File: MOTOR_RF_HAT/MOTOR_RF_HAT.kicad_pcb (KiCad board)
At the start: 6 copper layers, 32 x 65 mm, 107 parts, among them J1 SMA, J2 SMA, J3 Raspberry_Pi_2_3, J4 Conn_01x01, J5 Conn_01x01, Q1 BSS138, U1 CC1200RHBR, U2 CC1200RHBR, U3 RaspberryPi_Pico, U4 XT30PW-M, U5 LMR51420YFDDCR, Y1 40MHz, Y2 40MHz

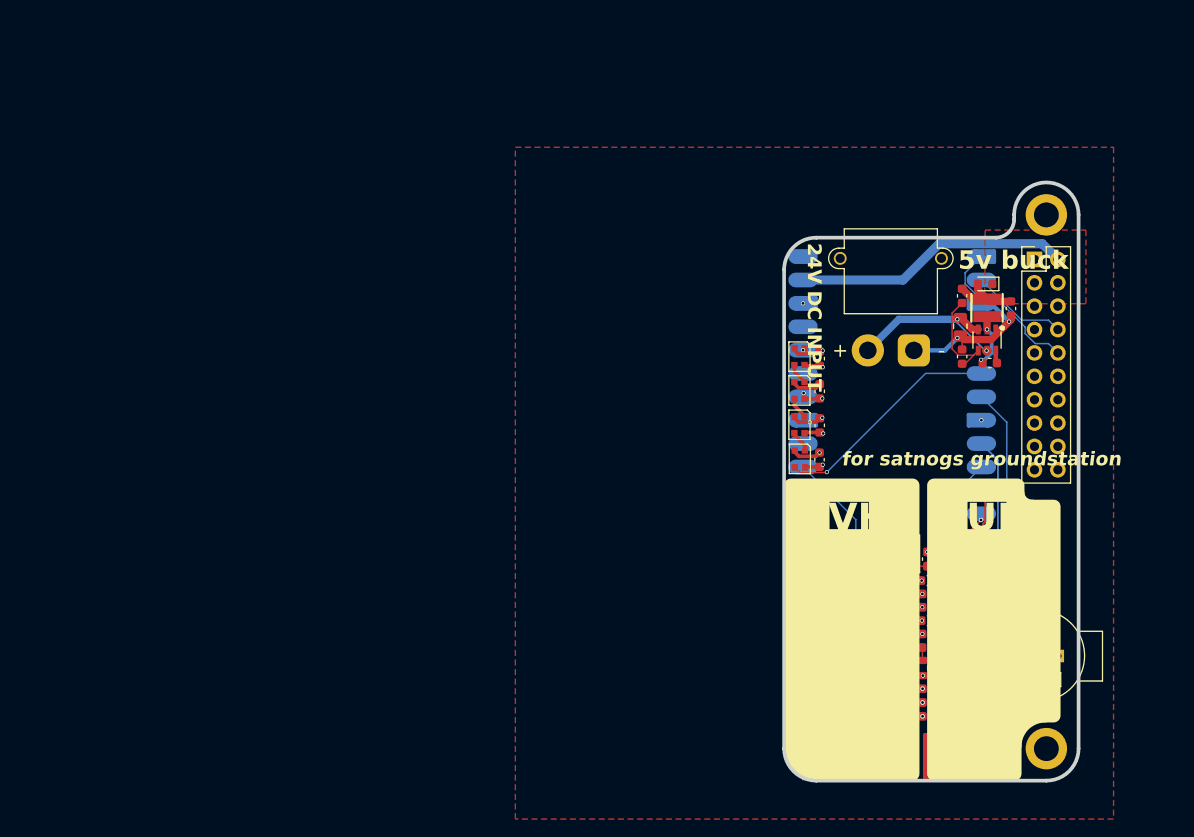
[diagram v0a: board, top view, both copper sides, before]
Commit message: MOTOR_RF_HAT: assign components:smallpad to all TestPoint_Small
Assigned local smallpad footprint to 8 TestPoint_Small instances:
- 7 in solder_pads.kicad_sch
- 1 in root schematic (TP19)

Co-Authored-By: Claude Opus 4.6 (1M context) <noreply@anthropic.com>
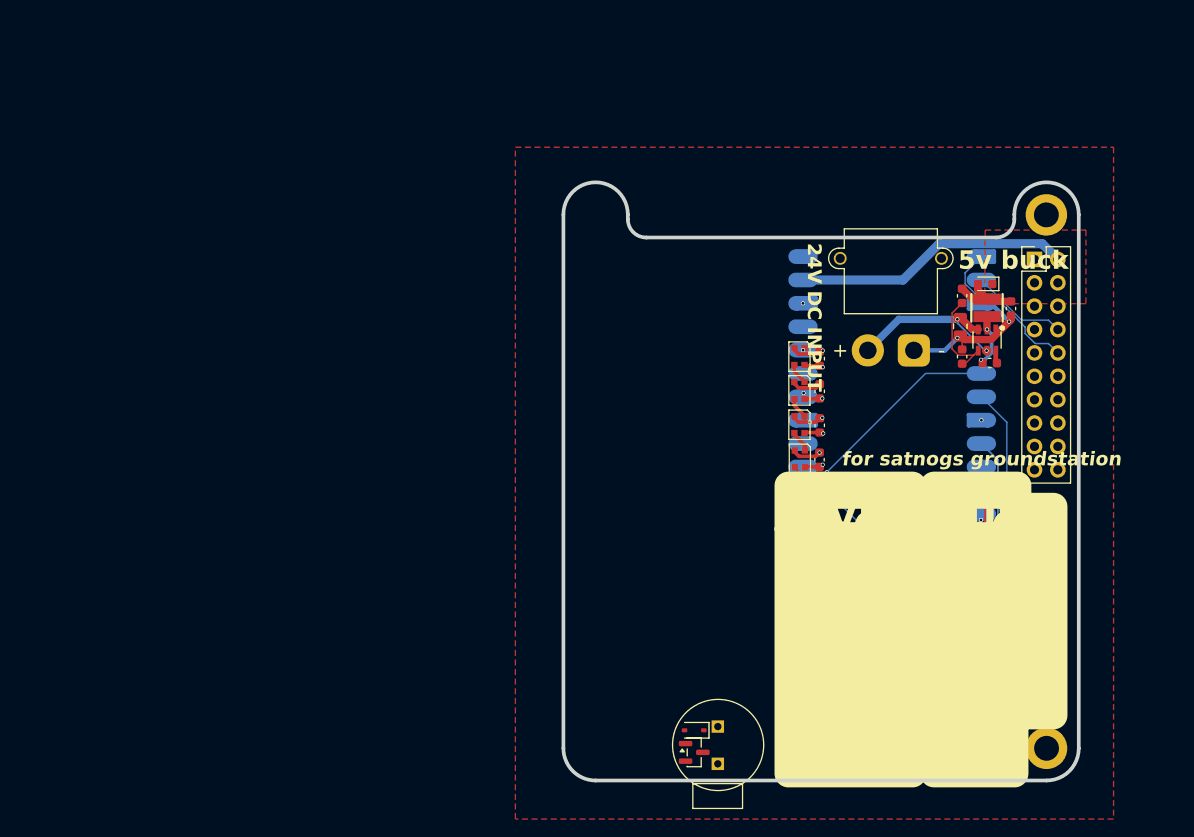
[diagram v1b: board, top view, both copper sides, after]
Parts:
- moved Q1 39.1 mm to (176.4, 122.8), turned to 0 degrees
- moved J5 38.8 mm to (179.0, 124.0), turned to 180 degrees
- moved D2 36.3 mm to (176.4, 120.4), turned to 180 degrees
- moved J4 33.8 mm to (179.0, 120.0), turned to 180 degrees
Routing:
- net Net-(D2-A): track 5.55 -> 0.00 mm
- net +3V3: track 66.8 -> 65.1 mm, vias 36 -> 35
- net GND: vias 63 -> 62
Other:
- board size 32 x 65 mm -> 56 x 65 mm

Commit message: MOTOR_RF_HAT: add TestPoint lib alias to fix persistent smallpad errors
KiCad's lib_symbols cache keeps reverting footprint refs to
TestPoint:smallpad on save. Added TestPoint as a footprint library
alias pointing to components.pretty so both TestPoint:smallpad and
components:smallpad resolve to the same local footprint.

Co-Authored-By: Claude Opus 4.6 (1M context) <noreply@anthropic.com>
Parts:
- added C60: 10uF, Capacitor_SMD:C_0805_2012Metric_Pad1.18x1.45mm_HandSolder, F.Cu at (120.2, 100.6)
- added C61: 10uF, Capacitor_SMD:C_0805_2012Metric_Pad1.18x1.45mm_HandSolder, F.Cu at (120.2, 103.6)
- added C62: 10uF, Capacitor_SMD:C_0805_2012Metric_Pad1.18x1.45mm_HandSolder, F.Cu at (120.2, 106.7)
- added C63: 100nF, Capacitor_SMD:C_0805_2012Metric_Pad1.18x1.45mm_HandSolder, F.Cu at (120.2, 109.7)
- added C64: 10uF, Capacitor_SMD:C_0805_2012Metric_Pad1.18x1.45mm_HandSolder, F.Cu at (104.9, 100.6)
- added C65: 10uF, Capacitor_SMD:C_0805_2012Metric_Pad1.18x1.45mm_HandSolder, F.Cu at (104.9, 103.6)
- added C66: 10uF, Capacitor_SMD:C_0805_2012Metric_Pad1.18x1.45mm_HandSolder, F.Cu at (104.9, 106.7)
- added C67: 100nF, Capacitor_SMD:C_0805_2012Metric_Pad1.18x1.45mm_HandSolder, F.Cu at (104.9, 109.7)
- added C68: 100nF, Capacitor_SMD:C_0805_2012Metric_Pad1.18x1.45mm_HandSolder, F.Cu at (123.7, 73.0)
- added C69: 100nF, Capacitor_SMD:C_0805_2012Metric_Pad1.18x1.45mm_HandSolder, F.Cu at (123.7, 76.0)
- added C70: 100nF, Capacitor_SMD:C_0805_2012Metric_Pad1.18x1.45mm_HandSolder, F.Cu at (123.7, 79.0)
- added C71: 100nF, Capacitor_SMD:C_0805_2012Metric_Pad1.18x1.45mm_HandSolder, F.Cu at (123.7, 82.0)
- added H3: MountingHole_Pad, MountingHole:MountingHole_2.7mm_M2.5_ISO7380_Pad, F.Cu at (131.1, 74.5)
- added H4: MountingHole_Pad, MountingHole:MountingHole_2.7mm_M2.5_ISO7380_Pad, F.Cu at (131.1, 80.6)
- added J6: JST_AZ, components:CONN-TH_S6B-XH-A-LF-SN, F.Cu at (111.9, 81.4)
- added J7: JST_EL, components:CONN-TH_S6B-XH-A-LF-SN, F.Cu at (111.9, 94.2)
- added R11: 100R, Resistor_SMD:R_0805_2012Metric_Pad1.20x1.40mm_HandSolder, F.Cu at (123.7, 85.0)
- added R12: 100R, Resistor_SMD:R_0805_2012Metric_Pad1.20x1.40mm_HandSolder, F.Cu at (123.7, 88.0)
- added R13: 100R, Resistor_SMD:R_0805_2012Metric_Pad1.20x1.40mm_HandSolder, F.Cu at (123.7, 90.9)
- added R14: 100R, Resistor_SMD:R_0805_2012Metric_Pad1.20x1.40mm_HandSolder, F.Cu at (123.7, 93.9)
- added TP1: TestPoint_Small, components:smallpad, F.Cu at (136.2, 75.4)
- added U6: A4950E, components:SOIC-8-1EP_3.9x4.9mm_P1.27mm_EP2.41x3.3mm, F.Cu at (126.8, 102.5)
- added U7: A4950E, components:SOIC-8-1EP_3.9x4.9mm_P1.27mm_EP2.41x3.3mm, F.Cu at (111.5, 102.5)
- moved D1 71.8 mm to (136.2, 72.8), turned to 0 degrees
- renumbered C19 to C1, C20 to C10, C23 to C11, C13 to C12, C18 to C13, C25 to C14, C26 to C15, C27 to C16, C28 to C17, C29 to C18, C30 to C19, C22 to C2, C15 to C20, C31 to C21, C21 to C22, C32 to C23, C8 to C24, C33 to C25, C14 to C26, C57 to C27, C34 to C28, C35 to C29, C24 to C3, C58 to C30, C16 to C31, C36 to C32, C9 to C33, C59 to C34, C37 to C35, C17 to C36, C38 to C37, C60 to C38, C48 to C4, C61 to C42, C42 to C43, C43 to C44, C44 to C45, C62 to C46, C5 to C47, C45 to C48, C2 to C49, C49 to C5, C63 to C50, C6 to C51, C46 to C52, C64 to C53, C7 to C54, C1 to C55, C47 to C56, C3 to C57, C4 to C58, C10 to C59, C50 to C6, C51 to C7, C11 to C8, C12 to C9, D3 to D2, D2 to D3, H4 to H2, J4 to J1, J5 to J2, J2 to J4, J1 to J5, L18 to L1, L13 to L10, L4 to L11, L14 to L12, L15 to L13, L16 to L14, L1 to L15, L2 to L16, L3 to L17, L9 to L2, L10 to L3, L11 to L4, L12 to L5, L5 to L8, L8 to L9, R16 to R1, R6 to R10, R17 to R2, R1 to R3, R2 to R5, R3 to R6, R5 to R7, R7 to R8, R8 to R9, U4 to U1, U5 to U2, U2 to U3, U3 to U4, U1 to U5, Y2 to Y1, Y1 to Y2
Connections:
- C3 pad 1: +5V_BUCK -> +5V
- D1 pad 1: +5V -> /4.5V
- D1 pad 2: +5V_BUCK -> +5V
- D2 pad 4: +3V3 -> /4.5V
- D4 pad 4: +3V3 -> /4.5V
- D5 pad 4: +3V3 -> /4.5V
- D6 pad 4: +3V3 -> /4.5V
- L1 pad 2: +5V_BUCK -> +5V
- R1 pad 2: +5V_BUCK -> +5V
- U4 pad 20: unconnected-(U3-GPIO15-Pad20) -> /Pico_SPI_Host/AZ_ENC_B
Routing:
- net +5V_BUCK: track 7.93 -> 0.00 mm
- net +5V: track 30.0 -> 38.0 mm

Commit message: MOTOR_RF_HAT: fix cap packages — 10uF/50V, 22uF, 4.7uF/50V back to 0805
These values cannot physically fit in 0603:
- C1 (4.7uF 50V): 0603→0805
- C3 (22uF): 0603→0805
- C60-C62 (10uF AZ motor VBB bypass): 0603→0805
- C64-C66 (10uF EL motor VBB bypass): 0603→0805

All other passives remain 0603.

Co-Authored-By: Claude Opus 4.6 (1M context) <noreply@anthropic.com>
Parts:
- added TP10: ~, components:smallpad, F.Cu at (108.5, 46.4)
- added TP11: ~, components:smallpad, F.Cu at (108.5, 49.0)
- added TP12: ~, components:smallpad, F.Cu at (108.5, 51.6)
- added TP13: ~, components:smallpad, F.Cu at (108.5, 54.2)
- added TP14: ~, components:smallpad, F.Cu at (108.5, 56.8)
- added TP15: ~, components:smallpad, F.Cu at (108.5, 59.4)
- added TP16: ~, components:smallpad, F.Cu at (112.5, 43.8)
- added TP17: ~, components:smallpad, F.Cu at (112.5, 46.4)
- added TP18: ~, components:smallpad, F.Cu at (112.5, 49.0)
- added TP19: ~, components:smallpad, F.Cu at (112.5, 51.6)
- added TP2: ~, components:smallpad, F.Cu at (104.5, 43.8)
- added TP3: ~, components:smallpad, F.Cu at (104.5, 46.4)
- added TP4: ~, components:smallpad, F.Cu at (104.5, 49.0)
- added TP5: ~, components:smallpad, F.Cu at (104.5, 51.6)
- added TP6: ~, components:smallpad, F.Cu at (104.5, 54.2)
- added TP7: ~, components:smallpad, F.Cu at (104.5, 56.8)
- added TP8: ~, components:smallpad, F.Cu at (104.5, 59.4)
- added TP9: ~, components:smallpad, F.Cu at (108.5, 43.8)

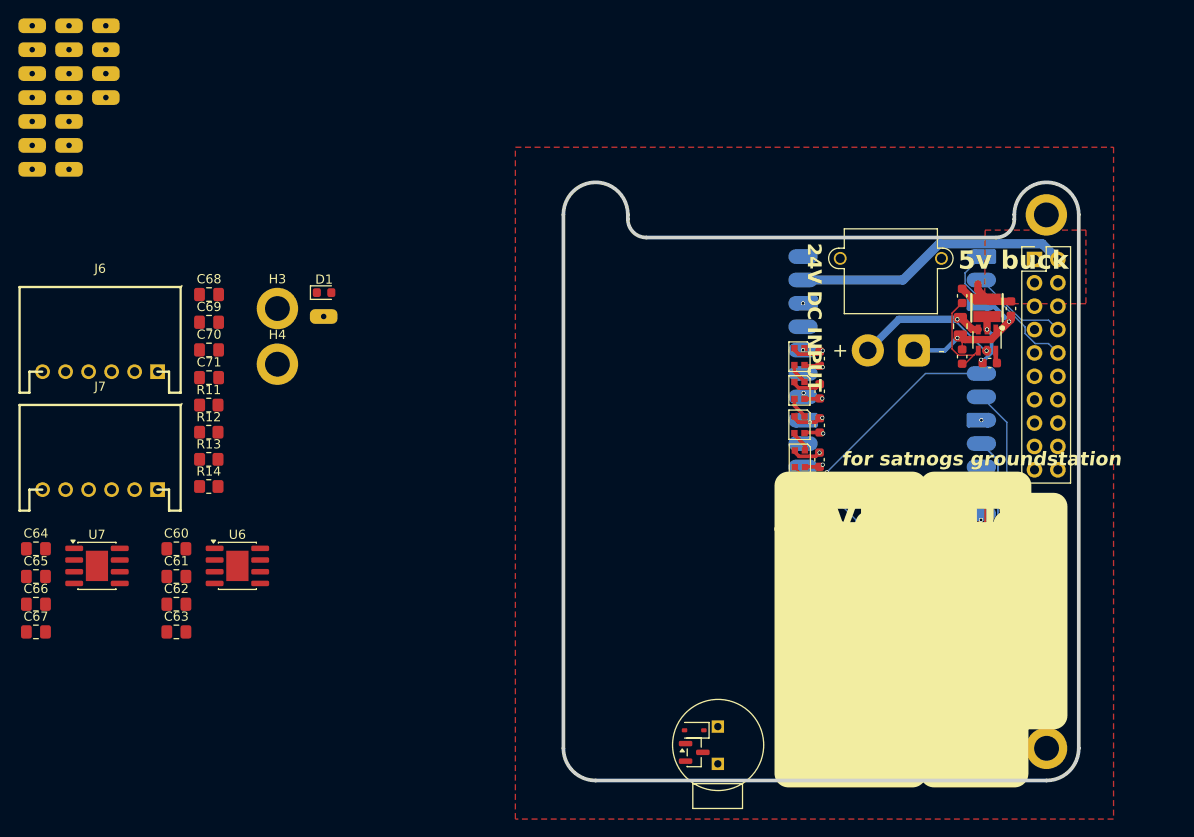
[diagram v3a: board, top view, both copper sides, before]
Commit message: MOTOR_RF_HAT: fix all 3D model paths in footprints and PCB
Fixed 3D model references in local footprints:
- JST 2/6-pin: components.pretty → components.3dshapes
- XT30PW-M: packages3d/ → ${KIPRJMOD}/components.3dshapes/
- SOT-23-6 (LMR51420): lib.3dshapes → components.3dshapes
- Inductor: lib.3dshapes → components.3dshapes
- Beeper: components.pretty → components.3dshapes
- HSOP-16: ${EASYEDA2KICAD} → components.3dshapes

Also fixed same paths in MOTOR_RF_HAT.kicad_pcb.

A4950 (SOIC-8-EP) and JST-XH 4-pin use KiCad global 3D models
which resolve correctly via ${KICAD10_3DMODEL_DIR}.

WS2812B-2020 has no 3D model (cosmetic only, not blocking).

Co-Authored-By: Claude Opus 4.6 (1M context) <noreply@anthropic.com>
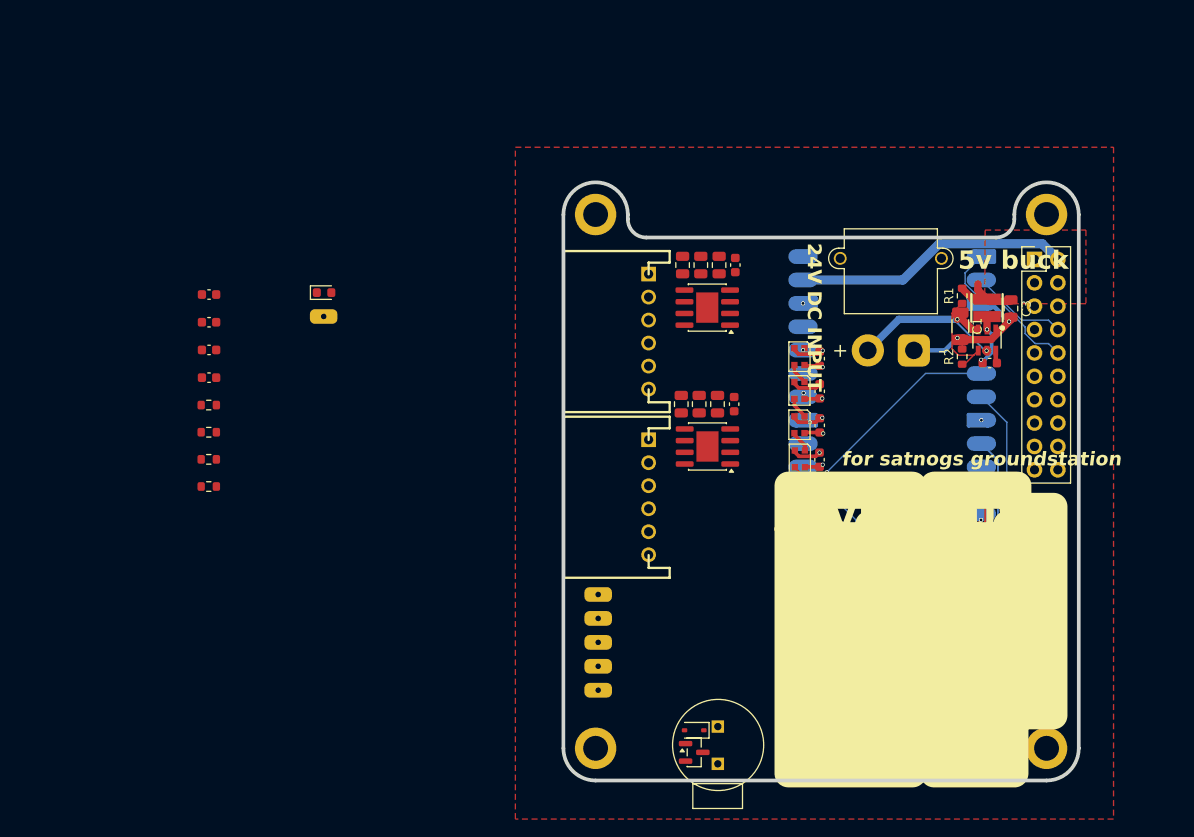
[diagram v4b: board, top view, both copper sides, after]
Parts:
- removed TP10, TP11, TP12, TP13, TP14, TP15, TP16, TP17, TP18, TP19, TP7, TP8, TP9: ~, components:smallpad
- C1: footprint Capacitor_SMD:C_0805_2012Metric -> Capacitor_SMD:C_1206_3216Metric
- C3: footprint Capacitor_SMD:C_0603_1608Metric -> Capacitor_SMD:C_0805_2012Metric
- C60, C61, C62, C64, C65, C66: footprint Capacitor_SMD:C_0805_2012Metric_Pad1.18x1.45mm_HandSolder -> Capacitor_SMD:C_0805_2012Metric
- C63, C67: footprint Capacitor_SMD:C_0805_2012Metric_Pad1.18x1.45mm_HandSolder -> Capacitor_SMD:C_0603_1608Metric
- C68, C69, C70, C71: value 100nF -> 100pF; footprint Capacitor_SMD:C_0805_2012Metric_Pad1.18x1.45mm_HandSolder -> Capacitor_SMD:C_0603_1608Metric
- R1, R2: footprint Capacitor_SMD:C_0603_1608Metric -> Resistor_SMD:R_0603_1608Metric
- R11, R12, R13, R14: footprint Resistor_SMD:R_0805_2012Metric_Pad1.20x1.40mm_HandSolder -> Resistor_SMD:R_0603_1608Metric
- TP1: value TestPoint_Small -> MISO
- TP2: value ~ -> MOSI
- TP3: value ~ -> CLK
- TP4: value ~ -> CS
- TP5: value ~ -> 3.3V
- TP6: value ~ -> GND
- moved TP3 87.2 mm to (166.0, 108.2)
- moved TP5 87.2 mm to (166.0, 113.4)
- moved TP2 87.2 mm to (166.0, 105.6)
- moved TP4 87.2 mm to (166.0, 110.8)
- moved TP6 87.2 mm to (166.0, 116.0)
- moved C67 85.8 mm to (180.9, 69.8), turned to 90 degrees
- moved C66 82.9 mm to (179.1, 69.8), turned to 90 degrees
- moved C65 79.8 mm to (177.2, 69.8), turned to 90 degrees
- moved C64 76.7 mm to (175.2, 69.8), turned to 90 degrees
- moved U7 72.0 mm to (177.8, 74.4), turned to 180 degrees
- moved C63 65.5 mm to (180.8, 84.9), turned to 90 degrees
- moved C62 62.7 mm to (179.0, 84.9), turned to 90 degrees
- moved J7 62.0 mm to (171.5, 77.0), turned to 90 degrees
- moved J6 61.1 mm to (171.5, 95.0), turned to 90 degrees
- moved C61 59.8 mm to (177.0, 84.9), turned to 90 degrees
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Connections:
- TP1 pad 1: unconnected-(TP1-Pad1) -> /CC1200_VHF_144MHz/VHF_MISO
- TP2 pad 1: /Solder_Pads/U0.TX -> /CC1200_VHF_144MHz/VHF_MOSI
- TP3 pad 1: /Solder_Pads/U0.RX -> /CC1200_VHF_144MHz/VHF_SCLK
- TP4 pad 1: GND -> /Pico_SPI_Host/IMU_CS
- TP6 pad 1: +5V -> GND
- U3 pad 10: /CC1200_VHF_144MHz/VHF_GPIO0 -> unconnected-(U3-GPIO0-Pad10)
- U3 pad 3: /CC1200_VHF_144MHz/VHF_GPIO3 -> unconnected-(U3-GPIO3-Pad3)
- U3 pad 4: /CC1200_VHF_144MHz/VHF_GPIO2 -> unconnected-(U3-GPIO2-Pad4)
- U4 pad 12: /CC1200_UHF_432MHz/UHF_GPIO2 -> unconnected-(U4-GPIO9-Pad12)
- U4 pad 20: /Pico_SPI_Host/AZ_ENC_B -> /Encoders/EL_ENC_A
- U4 pad 27: /CC1200_VHF_144MHz/VHF_GPIO2 -> /Encoders/AZ_ENC_B
- U4 pad 29: /CC1200_VHF_144MHz/VHF_GPIO0 -> /Encoders/EL_ENC_B
- U4 pad 31: /CC1200_VHF_144MHz/VHF_GPIO3 -> /Pico_SPI_Host/IMU_CS
- U4 pad 32: unconnected-(U4-GPIO27_ADC1-Pad32) -> /Elevation/EL_EN/IN1
- U4 pad 34: unconnected-(U4-GPIO28_ADC2-Pad34) -> /Elevation/EL_PH/IN2
- U4 pad 39: +5V -> unconnected-(U4-VSYS-Pad39)
- U4 pad 6: /WS2812B -> /Pico_SPI_Host/WS2812
- U4 pad 9: /CC1200_UHF_432MHz/UHF_GPIO3 -> unconnected-(U4-GPIO6-Pad9)
- U5 pad 3: /CC1200_UHF_432MHz/UHF_GPIO3 -> unconnected-(U5-GPIO3-Pad3)
- U5 pad 4: /CC1200_UHF_432MHz/UHF_GPIO2 -> unconnected-(U5-GPIO2-Pad4)
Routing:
- net (no net): track 0.00 -> 38.4 mm, vias 0 -> 3
- net /CC1200_UHF_432MHz/UHF_GPIO3: track 16.7 -> 0.00 mm, vias 1 -> 0
- net /CC1200_VHF_144MHz/VHF_GPIO3: track 14.1 -> 0.00 mm, vias 1 -> 0
- net /Encoders/EL_ENC_B: track 0.00 -> 9.16 mm, vias 0 -> 1
- net /CC1200_VHF_144MHz/VHF_GPIO0: track 9.16 -> 0.00 mm, vias 1 -> 0
- net /Encoders/AZ_ENC_B: track 0.00 -> 7.66 mm, vias 0 -> 2
- net /CC1200_VHF_144MHz/VHF_GPIO2: track 7.66 -> 0.00 mm, vias 2 -> 0
- net /CC1200_UHF_432MHz/UHF_GPIO2: track 7.59 -> 0.00 mm, vias 1 -> 0
- net unconnected-(U4-GPIO28_ADC2-Pad34): vias 1 -> 0
- net /Elevation/EL_PH/IN2: vias 0 -> 1
